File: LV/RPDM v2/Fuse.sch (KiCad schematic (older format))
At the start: 3 parts

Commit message: RPDM v2 nearly done
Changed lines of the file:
@@
 $Descr A4 11693 8268
 encoding utf-8
-Sheet 25 28
+Sheet 24 29
 Title "Fuse Circuit"
-Date "2020-02-27"
-Rev "1"
+Date "2021-06-28"
+Rev "2"
 Comp "UOW Motorsport"
 Comment1 ""
 Comment2 ""
-Comment3 "Brandon Shaw"
+Comment3 "Brandon Shaw, Joshua Smedley"
 Comment4 "Design By:"
 $EndDescr
@@
 AR Path="/5E554D5D/60DED791/5E574E2C" Ref="F?"  Part="1"
 AR Path="/5E554D5D/60DEDCBD/5E574E2C" Ref="F?"  Part="1"
+AR Path="/60D73B14/5E574E2C" Ref="F?"  Part="1"
+AR Path="/5E553FD7/61029B48/5E574E2C" Ref="F?"  Part="1"
+AR Path="/5E553FD7/61029C97/5E574E2C" Ref="F?"  Part="1"
+AR Path="/5E553C05/6121AD04/5E574E2C" Ref="F?"  Part="1"
+AR Path="/5E553C05/60E9D8C7/5E574E2C" Ref="F?"  Part="1"
+AR Path="/5E553C05/60E9D8CB/5E574E2C" Ref="F?"  Part="1"
+AR Path="/5E553C05/60E9D8D5/5E574E2C" Ref="F?"  Part="1"
+AR Path="/5E553C05/60E9D8D9/5E574E2C" Ref="F?"  Part="1"
+AR Path="/5E553C05/60E9D8E3/5E574E2C" Ref="F?"  Part="1"
 F 0 "F?" H 4610 3246 50  0000 L CNN
 F 1 "Fuse" H 4610 3155 50  0000 L CNN
@@
 	1    0    0    -1
 $EndComp
-Text HLabel 4550 3850 3    50   Input ~ 0
+Text HLabel 4550 3850 3    50   Output ~ 0
 Fuse_Out
 Text HLabel 4550 2650 1    50   Input ~ 0
@@
 AR Path="/5E554D5D/60DED791/5E57CF75" Ref="#PWR?"  Part="1"
 AR Path="/5E554D5D/60DEDCBD/5E57CF75" Ref="#PWR?"  Part="1"
+AR Path="/60D73B14/5E57CF75" Ref="#PWR?"  Part="1"
+AR Path="/5E553FD7/61029B48/5E57CF75" Ref="#PWR?"  Part="1"
+AR Path="/5E553FD7/61029C97/5E57CF75" Ref="#PWR?"  Part="1"
+AR Path="/5E553C05/6121AD04/5E57CF75" Ref="#PWR?"  Part="1"
+AR Path="/5E553C05/60E9D8C7/5E57CF75" Ref="#PWR?"  Part="1"
+AR Path="/5E553C05/60E9D8CB/5E57CF75" Ref="#PWR?"  Part="1"
+AR Path="/5E553C05/60E9D8D5/5E57CF75" Ref="#PWR?"  Part="1"
+AR Path="/5E553C05/60E9D8D9/5E57CF75" Ref="#PWR?"  Part="1"
+AR Path="/5E553C05/60E9D8E3/5E57CF75" Ref="#PWR?"  Part="1"
 F 0 "#PWR?" H 5600 3400 50  0001 C CNN
 F 1 "GND" H 5605 3477 50  0000 C CNN
@@
 AR Path="/5E554D5D/60DED791/5E5770E7" Ref="R?"  Part="1"
 AR Path="/5E554D5D/60DEDCBD/5E5770E7" Ref="R?"  Part="1"
+AR Path="/60D73B14/5E5770E7" Ref="R?"  Part="1"
+AR Path="/5E553FD7/61029B48/5E5770E7" Ref="R?"  Part="1"
+AR Path="/5E553FD7/61029C97/5E5770E7" Ref="R?"  Part="1"
+AR Path="/5E553C05/6121AD04/5E5770E7" Ref="R?"  Part="1"
+AR Path="/5E553C05/60E9D8C7/5E5770E7" Ref="R?"  Part="1"
+AR Path="/5E553C05/60E9D8CB/5E5770E7" Ref="R?"  Part="1"
+AR Path="/5E553C05/60E9D8D5/5E5770E7" Ref="R?"  Part="1"
+AR Path="/5E553C05/60E9D8D9/5E5770E7" Ref="R?"  Part="1"
+AR Path="/5E553C05/60E9D8E3/5E5770E7" Ref="R?"  Part="1"
 F 0 "R?" V 4800 3550 50  0000 C CNN
 F 1 "22k" V 5000 3550 50  0000 C CNN
@@
 AR Path="/5E554D5D/60DED791/5E57B77F" Ref="D?"  Part="1"
 AR Path="/5E554D5D/60DEDCBD/5E57B77F" Ref="D?"  Part="1"
+AR Path="/60D73B14/5E57B77F" Ref="D?"  Part="1"
+AR Path="/5E553FD7/61029B48/5E57B77F" Ref="D?"  Part="1"
+AR Path="/5E553FD7/61029C97/5E57B77F" Ref="D?"  Part="1"
+AR Path="/5E553C05/6121AD04/5E57B77F" Ref="D?"  Part="1"
+AR Path="/5E553C05/60E9D8C7/5E57B77F" Ref="D?"  Part="1"
+AR Path="/5E553C05/60E9D8CB/5E57B77F" Ref="D?"  Part="1"
+AR Path="/5E553C05/60E9D8D5/5E57B77F" Ref="D?"  Part="1"
+AR Path="/5E553C05/60E9D8D9/5E57B77F" Ref="D?"  Part="1"
+AR Path="/5E553C05/60E9D8E3/5E57B77F" Ref="D?"  Part="1"
 F 0 "D?" H 5350 3450 50  0000 C CNN
 F 1 "OK_LED" H 5350 3650 50  0000 C CNN

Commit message: rpdm
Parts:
- gave numbers to parts that had none: 3

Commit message: rpdm
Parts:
- R1: renamed from R401; value 22k -> 10k
- renumbered D401 to D1, F401 to F2
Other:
- moved on the sheet: D20, F21, R20

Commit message: rPDM - Started on board layout
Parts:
- D12: renamed from D1; footprint (none) -> Diode_SMD:D_0603_1608Metric_Pad1.05x0.95mm_HandSolder
- F1: renamed from F2; footprint (none) -> Fuse:Fuseholder_Blade_Mini_Keystone_3568
- R18: renamed from R1; footprint (none) -> Resistor_SMD:R_0805_2012Metric_Pad1.15x1.40mm_HandSolder

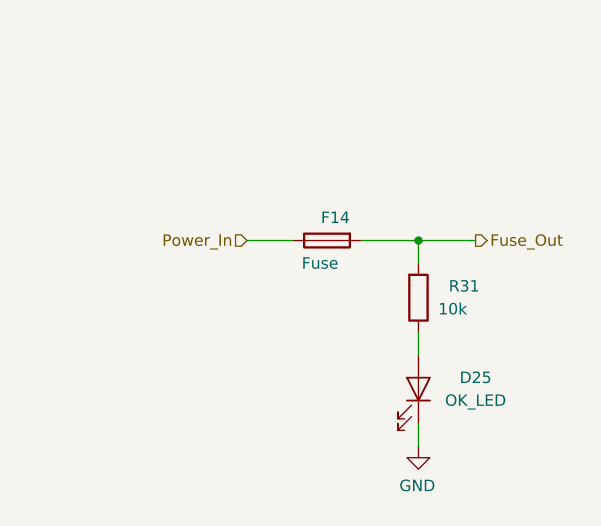
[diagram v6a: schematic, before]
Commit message: rpdm, libraries cleanup
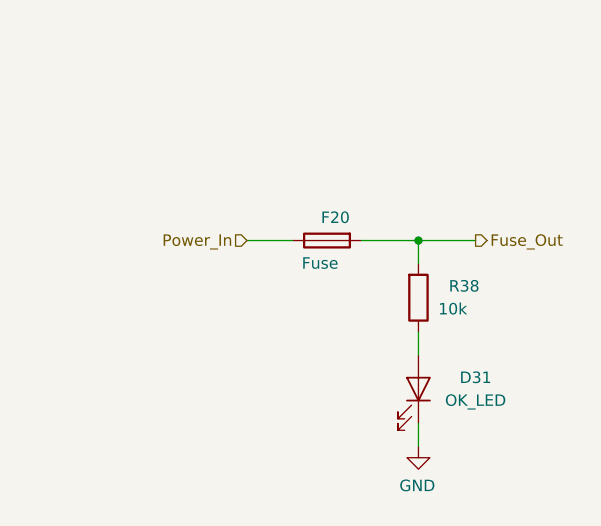
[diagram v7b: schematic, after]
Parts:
- renumbered R18 to R19
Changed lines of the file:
@@
 AR Path="/5E553C05/618E952A/5E574E2C" Ref="F19"  Part="1"
 AR Path="/5E553C05/618E952E/5E574E2C" Ref="F20"  Part="1"
-F 0 "F14" V 5750 3050 50  0000 L CNN
+F 0 "F20" V 5750 3050 50  0000 L CNN
 F 1 "Fuse" V 5950 3100 50  0000 L CNN
 F 2 "Fuse:Fuseholder_Blade_Mini_Keystone_3568" V 5780 3150 50  0001 C CNN
@@
 $EndComp
 $Comp
-L Device:R R18
+L Device:R R19
 U 1 1 5E5770E7
 P 6250 3400
-AR Path="/5E553C05/5E574CF7/5E5770E7" Ref="R18"  Part="1"
-AR Path="/5E553C05/5E58AB03/5E5770E7" Ref="R19"  Part="1"
-AR Path="/5E553C05/5E58ABE6/5E5770E7" Ref="R20"  Part="1"
-AR Path="/5E553C05/5E58ACF6/5E5770E7" Ref="R21"  Part="1"
-AR Path="/5E553C05/5E58ADD6/5E5770E7" Ref="R22"  Part="1"
-AR Path="/5E553C05/5E58AEC5/5E5770E7" Ref="R23"  Part="1"
-AR Path="/5E553C05/5E58AF99/5E5770E7" Ref="R24"  Part="1"
-AR Path="/5E553C05/5E58B05B/5E5770E7" Ref="R25"  Part="1"
-AR Path="/5E553C05/5E58C987/5E5770E7" Ref="R26"  Part="1"
-AR Path="/5E553C05/5E58C98B/5E5770E7" Ref="R27"  Part="1"
+AR Path="/5E553C05/5E574CF7/5E5770E7" Ref="R19"  Part="1"
+AR Path="/5E553C05/5E58AB03/5E5770E7" Ref="R20"  Part="1"
+AR Path="/5E553C05/5E58ABE6/5E5770E7" Ref="R21"  Part="1"
+AR Path="/5E553C05/5E58ACF6/5E5770E7" Ref="R22"  Part="1"
+AR Path="/5E553C05/5E58ADD6/5E5770E7" Ref="R23"  Part="1"
+AR Path="/5E553C05/5E58AEC5/5E5770E7" Ref="R24"  Part="1"
+AR Path="/5E553C05/5E58AF99/5E5770E7" Ref="R25"  Part="1"
+AR Path="/5E553C05/5E58B05B/5E5770E7" Ref="R26"  Part="1"
+AR Path="/5E553C05/5E58C987/5E5770E7" Ref="R27"  Part="1"
+AR Path="/5E553C05/5E58C98B/5E5770E7" Ref="R28"  Part="1"
 AR Path="/5E553C05/5E58C98F/5E5770E7" Ref="R?"  Part="1"
 AR Path="/5E553C05/5E58C993/5E5770E7" Ref="R?"  Part="1"
@@
 AR Path="/5E553C05/5E58CF1F/5E5770E7" Ref="R?"  Part="1"
 AR Path="/5E553C05/5E58CF23/5E5770E7" Ref="R?"  Part="1"
-AR Path="/5E553C05/5E65E6F4/5E5770E7" Ref="R28"  Part="1"
-AR Path="/5E553C05/5E65E6F8/5E5770E7" Ref="R29"  Part="1"
-AR Path="/5E553C05/5E789840/5E5770E7" Ref="R30"  Part="1"
-AR Path="/5E553C05/5E789844/5E5770E7" Ref="R31"  Part="1"
+AR Path="/5E553C05/5E65E6F4/5E5770E7" Ref="R29"  Part="1"
+AR Path="/5E553C05/5E65E6F8/5E5770E7" Ref="R30"  Part="1"
+AR Path="/5E553C05/5E789840/5E5770E7" Ref="R31"  Part="1"
+AR Path="/5E553C05/5E789844/5E5770E7" Ref="R32"  Part="1"
 AR Path="/5E554D5D/60DDF1D4/5E5770E7" Ref="R?"  Part="1"
 AR Path="/5E554D5D/60DE1E3F/5E5770E7" Ref="R?"  Part="1"
@@
 AR Path="/5E553FD7/61029B48/5E5770E7" Ref="R?"  Part="1"
 AR Path="/5E553FD7/61029C97/5E5770E7" Ref="R?"  Part="1"
-AR Path="/5E553C05/6121AD04/5E5770E7" Ref="R32"  Part="1"
-AR Path="/5E553C05/60E9D8C7/5E5770E7" Ref="R33"  Part="1"
-AR Path="/5E553C05/60E9D8CB/5E5770E7" Ref="R34"  Part="1"
+AR Path="/5E553C05/6121AD04/5E5770E7" Ref="R33"  Part="1"
+AR Path="/5E553C05/60E9D8C7/5E5770E7" Ref="R34"  Part="1"
+AR Path="/5E553C05/60E9D8CB/5E5770E7" Ref="R35"  Part="1"
 AR Path="/5E553C05/60E9D8D5/5E5770E7" Ref="R?"  Part="1"
 AR Path="/5E553C05/60E9D8D9/5E5770E7" Ref="R?"  Part="1"
 AR Path="/5E553C05/60E9D8E3/5E5770E7" Ref="R?"  Part="1"
-AR Path="/5E553C05/618E9522/5E5770E7" Ref="R35"  Part="1"
-AR Path="/5E553C05/618E952A/5E5770E7" Ref="R36"  Part="1"
-AR Path="/5E553C05/618E952E/5E5770E7" Ref="R37"  Part="1"
-F 0 "R31" H 6450 3350 50  0000 C CNN
+AR Path="/5E553C05/618E9522/5E5770E7" Ref="R36"  Part="1"
+AR Path="/5E553C05/618E952A/5E5770E7" Ref="R37"  Part="1"
+AR Path="/5E553C05/618E952E/5E5770E7" Ref="R38"  Part="1"
+F 0 "R38" H 6450 3350 50  0000 C CNN
 F 1 "10k" H 6400 3450 50  0000 C CNN
 F 2 "Resistor_SMD:R_0805_2012Metric_Pad1.15x1.40mm_HandSolder" V 6180 3400 50  0001 C CNN
@@
 AR Path="/5E553C05/618E952A/5E57B77F" Ref="D30"  Part="1"
 AR Path="/5E553C05/618E952E/5E57B77F" Ref="D31"  Part="1"
-F 0 "D25" V 6300 4050 50  0000 C CNN
+F 0 "D31" V 6300 4050 50  0000 C CNN
 F 1 "OK_LED" V 6200 4050 50  0000 C CNN
 F 2 "Diode_SMD:D_0603_1608Metric_Pad1.05x0.95mm_HandSolder" H 6250 3800 50  0001 C CNN

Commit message: RPDM
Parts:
- F1: footprint Fuse:Fuseholder_Blade_Mini_Keystone_3568 -> UOWM_Fuses:Keystone_3568
- renumbered D12 to D9, R19 to R16
